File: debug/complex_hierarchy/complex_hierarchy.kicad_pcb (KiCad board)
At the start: 2 copper layers, 100.7 x 80 mm, 68 parts, among them P1 CONN_2, P2 CONN_2, P3 CONN_2, P4 CONN_2, P5 CONN_2, P6 CONN_2, Q1 MPSA92, Q2 MPSA42, Q3 MPSA92, Q4 MPSA42, Q5 MPSA92, Q6 MPSA42, Q7 MPSA92, Q8 MPSA42, U1 ICL7660, U2 78L05, U3 LM358N, U4 LM358N

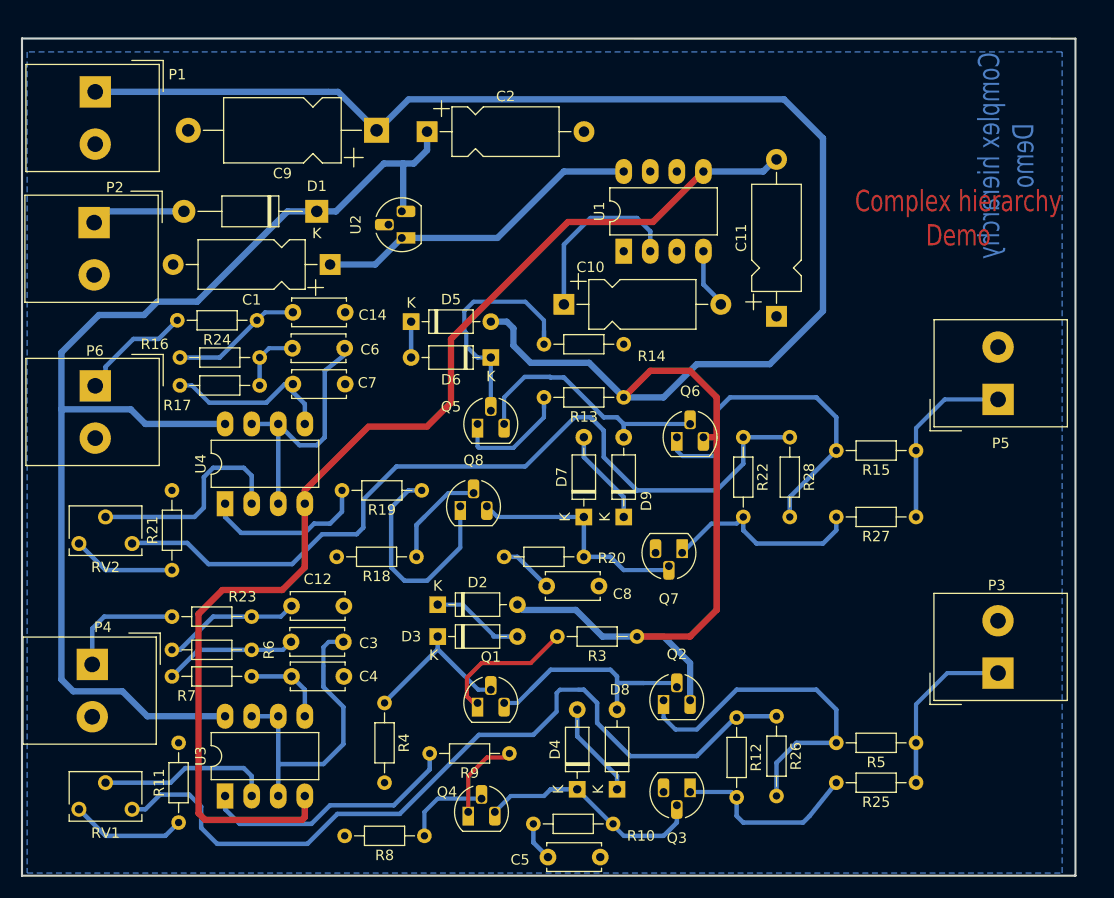
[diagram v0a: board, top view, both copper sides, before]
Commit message: Trying to fix the table header
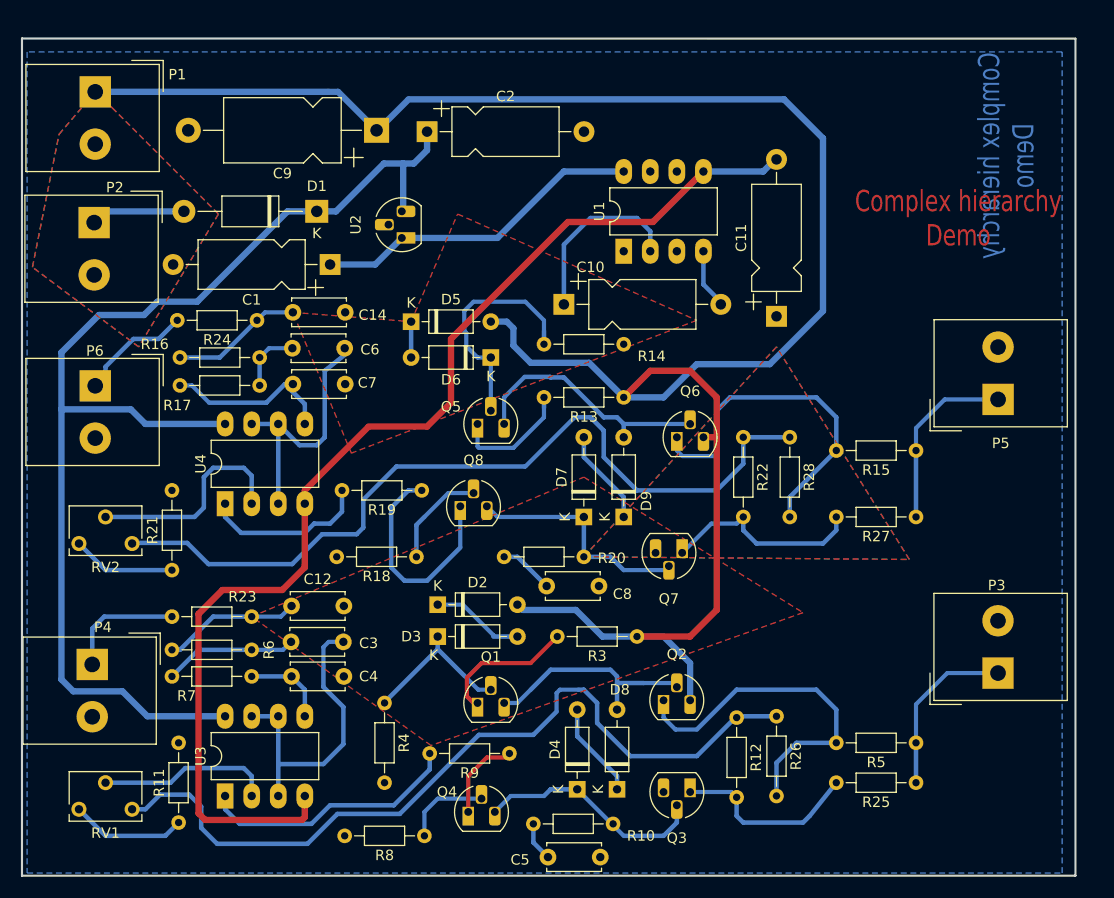
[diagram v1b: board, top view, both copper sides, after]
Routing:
- added copper zone on F.Cu, net +12V
- added copper zone on B.Cu, net /ampli_ht_horizontal/S_OUT+
- added copper zone on F.Cu, net /ampli_ht_horizontal/S_OUT+
- added copper zone on B.Cu, net /ampli_ht_vertical/PIEZO_IN
- added copper zone on F.Cu, net /ampli_ht_vertical/PIEZO_IN
- added copper zone on F.Cu, net /ampli_ht_vertical/Vpil_0_3,3V
- added copper zone on In1.Cu, net /ampli_ht_vertical/Vpil_0_3,3V
- added copper zone on In2.Cu, net /ampli_ht_vertical/Vpil_0_3,3V
- added copper zone on In3.Cu, net /ampli_ht_vertical/Vpil_0_3,3V
- added copper zone on In4.Cu, net /ampli_ht_vertical/Vpil_0_3,3V
- added copper zone on In5.Cu, net /ampli_ht_vertical/Vpil_0_3,3V
- added copper zone on In6.Cu, net /ampli_ht_vertical/Vpil_0_3,3V
- added copper zone on In7.Cu, net /ampli_ht_vertical/Vpil_0_3,3V
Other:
- copper layers 2 -> 20
